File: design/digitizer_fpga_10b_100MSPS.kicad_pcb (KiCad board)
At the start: 4 copper layers, 125 x 60 mm, 284 parts, among them J1 POWER, J2 SWD_01X04, J3 DEBUG_SPI, J4 USB_B_Mini, J5 SMA, J6 JUMPER_DFS/GAIN, J7 DEBUG_FPGA_GPIO, J8 DIGILENT_JTAG_HS2_01X06, SW1 RST, SW2 PROG, U1 LM3880MF-1AA, U10 IS61WV12816EDBLL-10TLI, U11 TLV431ACDBZR, U12 AD9214, U13 XC7S15-FTGB196, U14 IS25LP064A-JKx, U2 NCP59744MN1, U3 NCP59744MN1, U4 NCP59744MN1, U5 NCP59744MN1, U6 STM32H750VBTx, U7 USBLC6-2SC6, U8 FT231XS, U9 ADA4930-1, X1 ASTX-H11-25.000MHZ-T

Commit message: Added some layout
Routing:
- net /CLK: track 0.71 -> 133.3 mm, vias 1 -> 3
- net +3V3A: track 5.85 -> 29.4 mm, vias 22 -> 32
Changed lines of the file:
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@@
     (thickness 1.628)
     (drawings 36)
-    (tracks 1337)
+    (tracks 1399)
     (modules 284)
     (nets 354)
@@
   (gr_line (start 75 90) (end 190 90) (layer "Edge.Cuts") (width 0.05))
   (gr_line (start 70 145) (end 70 95) (layer "Edge.Cuts") (width 0.05))
+  (segment (start 108 117.5) (end 106.75 116.25) (width 0.2) (layer "BOT") (net 48))
+  (segment (start 106.75 112.75) (end 106.075 112.075) (width 0.2) (layer "BOT") (net 48))
+  (segment (start 106.75 116.25) (end 106.75 112.75) (width 0.2) (layer "BOT") (net 48))
+  (segment (start 111 115) (end 132.5 115) (width 0.2) (layer "BOT") (net 48))
+  (segment (start 108 124) (end 108 117.5) (width 0.2) (layer "BOT") (net 48))
+  (segment (start 110.5 115) (end 108 117.5) (width 0.2) (layer "BOT") (net 48))
+  (segment (start 111 115) (end 110.5 115) (width 0.2) (layer "BOT") (net 48))
+  (segment (start 106.075 112.075) (end 105.35 112.075) (width 0.2) (layer "BOT") (net 48))
+  (via (at 105.35 112.075) (size 0.35) (drill 0.1) (layers "TOP" "BOT") (net 48))
+  (segment (start 105.35 112.075) (end 103.9 112.075) (width 0.2) (layer "TOP") (net 48))
+  (segment (start 132.5 115) (end 133.5 114) (width 0.2) (layer "BOT") (net 48))
+  (segment (start 177 130) (end 177 132.5) (width 0.2) (layer "BOT") (net 48))
+  (segment (start 133.5 114) (end 133.5 113) (width 0.2) (layer "BOT") (net 48))
+  (segment (start 177 127.985) (end 177 130) (width 0.2) (layer "TOP") (net 48))
+  (segment (start 177 132.5) (end 162.5 147) (width 0.2) (layer "BOT") (net 48))
+  (segment (start 162.5 147) (end 131 147) (width 0.2) (layer "BOT") (net 48))
+  (segment (start 131 147) (end 108 124) (width 0.2) (layer "BOT") (net 48))
+  (segment (start 133.5 113) (end 134 112.5) (width 0.2) (layer "BOT") (net 48))
+  (via (at 177 130) (size 0.35) (drill 0.1) (layers "TOP" "BOT") (net 48))
+  (segment (start 102.5 107.525) (end 103.49 107.525) (width 0.5) (layer "BOT") (net 7))
+  (segment (start 103.49 107.525) (end 103.515 107.5) (width 0.5) (layer "BOT") (net 7))
+  (segment (start 103.515 108.035) (end 103.515 107.5) (width 0.5) (layer "BOT") (net 7))
+  (segment (start 103.515 108.5) (end 103.515 108.035) (width 0.5) (layer "BOT") (net 7))
+  (segment (start 102.5 108.175) (end 103.375 108.175) (width 0.5) (layer "BOT") (net 7))
+  (segment (start 103.375 108.175) (end 103.515 108.035) (width 0.5) (layer "BOT") (net 7))
+  (segment (start 102.5 111.425) (end 103.44 111.425) (width 0.5) (layer "BOT") (net 7))
+  (segment (start 103.44 111.425) (end 103.515 111.5) (width 0.5) (layer "BOT") (net 7))
+  (segment (start 103.125 112.725) (end 103.515 112.335) (width 0.5) (layer "BOT") (net 7))
+  (segment (start 103.515 112.335) (end 103.515 111.5) (width 0.5) (layer "BOT") (net 7))
+  (segment (start 102.5 112.725) (end 103.125 112.725) (width 0.5) (layer "BOT") (net 7))
+  (segment (start 102 112.725) (end 102.5 112.725) (width 0.5) (layer "BOT") (net 7))
+  (segment (start 102 111.425) (end 102.5 111.425) (width 0.5) (layer "BOT") (net 7))
+  (segment (start 102 108.175) (end 102.5 108.175) (width 0.5) (layer "BOT") (net 7))
+  (segment (start 102 107.525) (end 102.5 107.525) (width 0.5) (layer "BOT") (net 7))
+  (segment (start 103.4 106.5) (end 102.5 105.6) (width 0.5) (layer "BOT") (net 7))
+  (segment (start 103.515 106.5) (end 103.4 106.5) (width 0.5) (layer "BOT") (net 7))
+  (segment (start 102.5 105.6) (end 102.5 105.575) (width 0.5) (layer "BOT") (net 7))
+  (segment (start 102 105.575) (end 102.5 105.575) (width 0.5) (layer "BOT") (net 7))
+  (segment (start 103.515 107.5) (end 103.515 106.5) (width 0.5) (layer "BOT") (net 7))
+  (segment (start 103.515 109.5) (end 103.515 108.5) (width 0.5) (layer "BOT") (net 7))
+  (segment (start 103.515 110.5) (end 103.515 109.5) (width 0.5) (layer "BOT") (net 7))
+  (segment (start 103.515 111.5) (end 103.515 110.5) (width 0.5) (layer "BOT") (net 7))
+  (segment (start 103.9 112.725) (end 102.5 112.725) (width 0.25) (layer "TOP") (net 7))
+  (segment (start 102.5 112.725) (end 102 112.725) (width 0.25) (layer "TOP") (net 7))
+  (via (at 102.5 112.725) (size 0.35) (drill 0.1) (layers "TOP" "BOT") (net 7))
+  (via (at 102 112.725) (size 0.35) (drill 0.1) (layers "TOP" "BOT") (net 7))
+  (via (at 102.5 111.425) (size 0.35) (drill 0.1) (layers "TOP" "BOT") (net 7))
+  (segment (start 102.5 111.425) (end 102 111.425) (width 0.25) (layer "TOP") (net 7))
+  (segment (start 103.9 111.425) (end 102.5 111.425) (width 0.25) (layer "TOP") (net 7))
+  (via (at 102 111.425) (size 0.35) (drill 0.1) (layers "TOP" "BOT") (net 7))
+  (segment (start 103.9 108.175) (end 102.5 108.175) (width 0.25) (layer "TOP") (net 7))
+  (segment (start 102.5 108.175) (end 102 108.175) (width 0.25) (layer "TOP") (net 7))
+  (via (at 102.5 108.175) (size 0.35) (drill 0.1) (layers "TOP" "BOT") (net 7))
+  (via (at 102 108.175) (size 0.35) (drill 0.1) (layers "TOP" "BOT") (net 7))
+  (via (at 102.5 107.525) (size 0.35) (drill 0.1) (layers "TOP" "BOT") (net 7))
+  (segment (start 102.5 107.525) (end 102 107.525) (width 0.25) (layer "TOP") (net 7))
+  (segment (start 103.9 107.525) (end 102.5 107.525) (width 0.25) (layer "TOP") (net 7))
+  (via (at 102 107.525) (size 0.35) (drill 0.1) (layers "TOP" "BOT") (net 7))
+  (segment (start 103.9 105.575) (end 102.5 105.575) (width 0.25) (layer "TOP") (net 7))
+  (segment (start 102.5 105.575) (end 102 105.575) (width 0.25) (layer "TOP") (net 7))
+  (via (at 102.5 105.575) (size 0.35) (drill 0.1) (layers "TOP" "BOT") (net 7))
+  (via (at 102 105.575) (size 0.35) (drill 0.1) (layers "TOP" "BOT") (net 7))
   (segment (start 132.5 120.5) (end 134 119) (width 0.2) (layer "BOT") (net 82))
   (segment (start 125.5 120.5) (end 132.5 120.5) (width 0.2) (layer "BOT") (net 82))

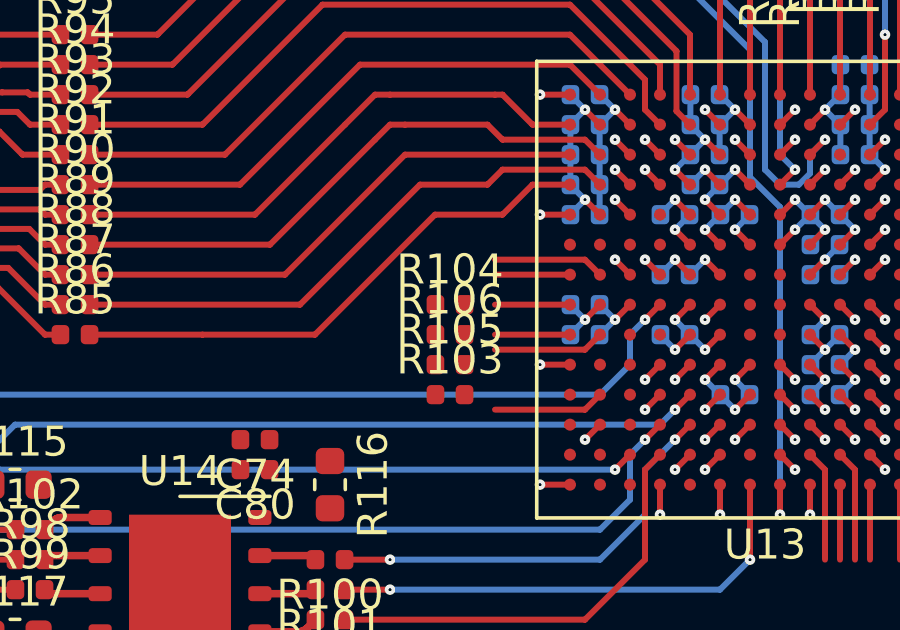
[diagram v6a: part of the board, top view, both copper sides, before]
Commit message: Rename buses from X..0 to 0..X
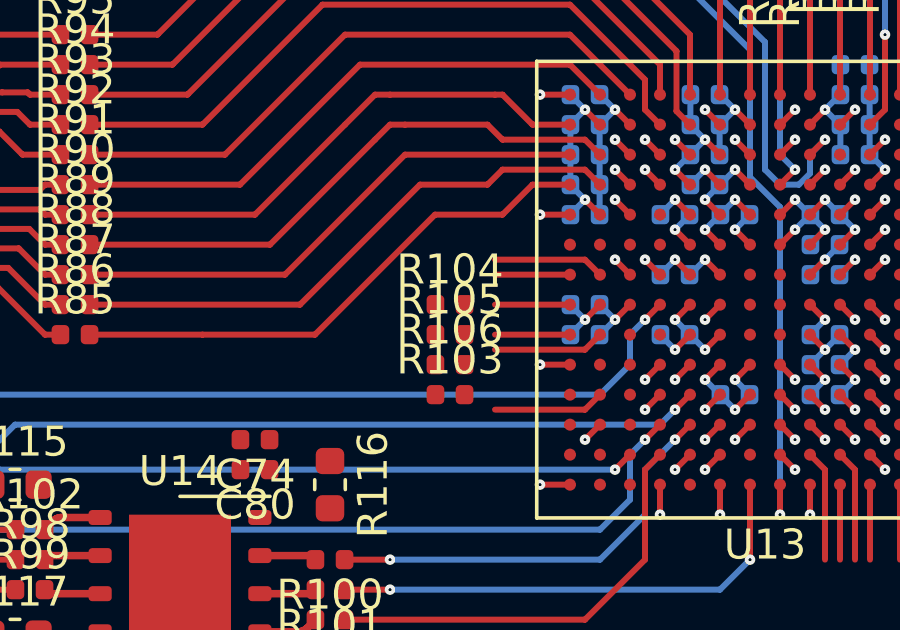
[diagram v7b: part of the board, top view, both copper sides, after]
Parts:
- moved R105 1.00 mm to (127.5, 113.0)
- moved R106 1.00 mm to (127.5, 114.0)
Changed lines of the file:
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@@
   )
   (module "Resistor_SMD:R_0402_1005Metric" (layer "TOP")
-    (at 127.5 113)
+    (at 127.5 114)
     (descr "Resistor SMD 0402 (1005 Metric), square (rectangular) end terminal, IPC_7351 nominal, (Body size source: http://www.tortai-tech.com/upload/download/2011102023233369053.pdf), generated with kicad-footprint-generator")
     (tags "resistor")
@@
   )
   (module "Resistor_SMD:R_0402_1005Metric" (layer "TOP")
-    (at 127.5 114)
+    (at 127.5 113)
     (descr "Resistor SMD 0402 (1005 Metric), square (rectangular) end terminal, IPC_7351 nominal, (Body size source: http://www.tortai-tech.com/upload/download/2011102023233369053.pdf), generated with kicad-footprint-generator")
     (tags "resistor")

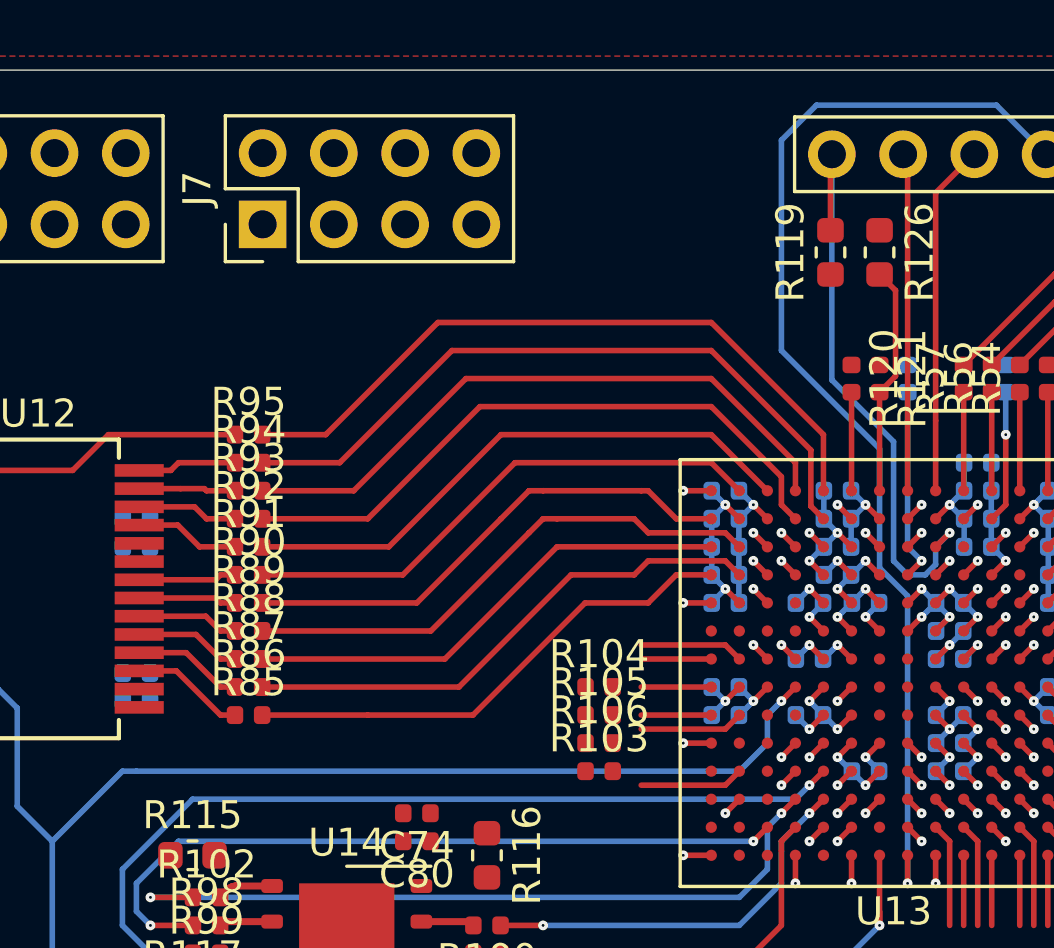
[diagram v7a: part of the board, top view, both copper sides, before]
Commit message: Updated ADC layout
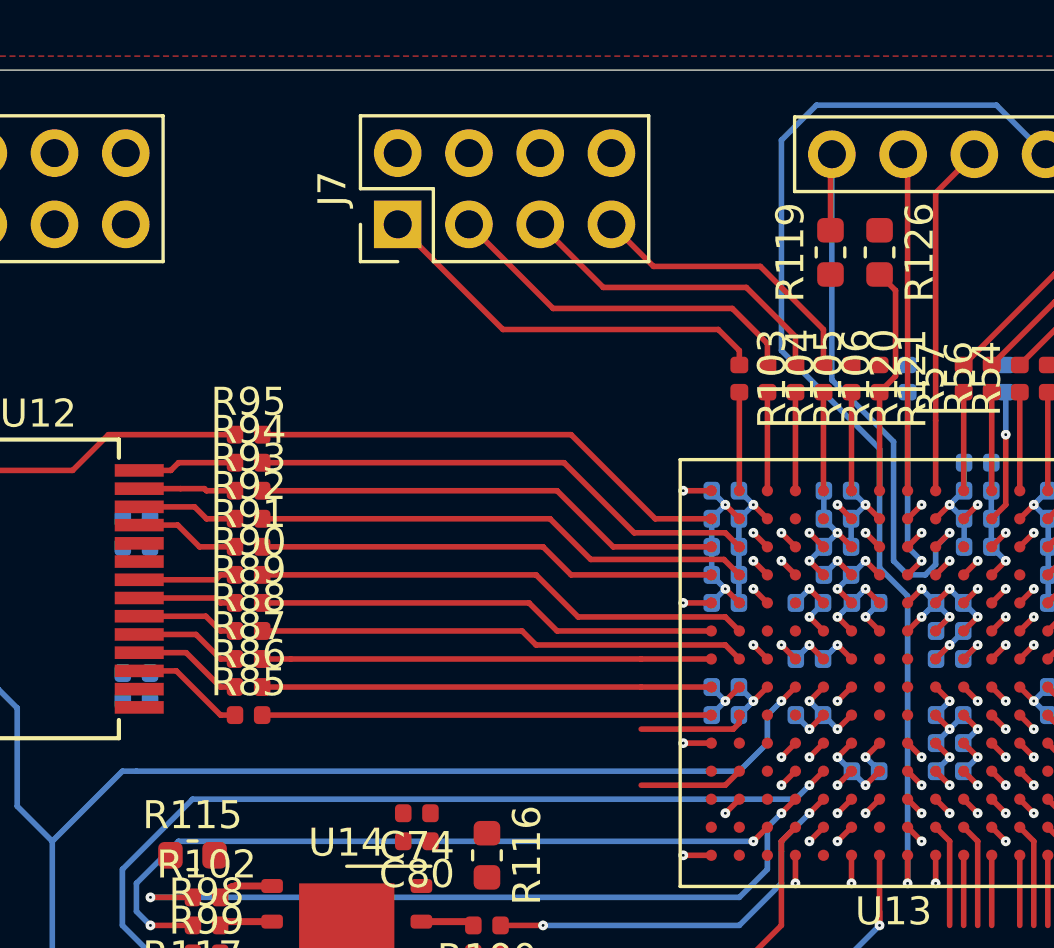
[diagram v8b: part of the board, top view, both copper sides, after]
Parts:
- moved R106 15.3 mm to (135.5, 101.0), turned to -90 degrees
- moved R103 14.9 mm to (132.5, 101.0), turned to -90 degrees
- moved R105 13.9 mm to (134.5, 101.0), turned to -90 degrees
- moved R104 12.5 mm to (133.5, 101.0), turned to -90 degrees
- moved J7 4.82 mm to (120.3, 95.5)
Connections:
- U13 pad D13: Net-(R103-Pad2) -> Net-(U13-PadD13)
- U13 pad F13: Net-(R106-Pad2) -> Net-(U13-PadF13)
- U13 pad F14: Net-(R105-Pad2) -> /ADC_DATA0
- U13 pad G14: Net-(R104-Pad2) -> /ADC_DATA1
- U13 pad H13: Net-(U13-PadH13) -> /ADC_DATA3
- U13 pad H14: Net-(U13-PadH14) -> /ADC_DATA2
- U13 pad J13: Net-(U13-PadJ13) -> /ADC_DATA5
- U13 pad J14: Net-(U13-PadJ14) -> /ADC_DATA4
- U13 pad L13: /ADC_DATA1 -> /ADC_DATA7
- U13 pad L14: /ADC_DATA0 -> /ADC_DATA6
- U13 pad M13: /ADC_DATA3 -> /ADC_DATA9
- U13 pad M14: /ADC_DATA2 -> /ADC_DATA8
- U13 pad N10: /ADC_DATA9 -> Net-(U13-PadN10)
- U13 pad N11: /ADC_DATA7 -> Net-(U13-PadN11)
- U13 pad N14: /ADC_DATA4 -> /ADC_OVRNG
- U13 pad P10: /ADC_OVRNG -> Net-(R106-Pad2)
- U13 pad P11: /ADC_DATA8 -> Net-(R105-Pad2)
- U13 pad P12: /ADC_DATA6 -> Net-(R104-Pad2)
- U13 pad P13: /ADC_DATA5 -> Net-(R103-Pad2)
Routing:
- net /FPGA/DEBUG_GPIO_0: track 0.00 -> 14.6 mm
- net /FPGA/DEBUG_GPIO_1: track 0.00 -> 13.2 mm
- net /FPGA/DEBUG_GPIO_2: track 0.00 -> 11.8 mm
- net /FPGA/DEBUG_GPIO_3: track 0.00 -> 10.4 mm
- net /ADC_OVRNG: track 25.3 -> 17.3 mm
- net /ADC_DATA9: track 25.3 -> 18.3 mm
- net /ADC_DATA8: track 22.9 -> 16.8 mm
- net /ADC_DATA7: track 22.9 -> 17.8 mm
- net /ADC_DATA6: track 20.5 -> 16.4 mm
- net Net-(U13-PadF13): track 0.00 -> 3.87 mm
- net Net-(U13-PadH13): track 3.71 -> 0.00 mm
- net Net-(U13-PadD13): track 0.00 -> 3.71 mm
- net /ADC_DATA1: track 19.1 -> 16.0 mm
- net Net-(U13-PadH14): track 2.50 -> 0.00 mm
- net /ADC_DATA0: track 18.1 -> 16.0 mm
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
